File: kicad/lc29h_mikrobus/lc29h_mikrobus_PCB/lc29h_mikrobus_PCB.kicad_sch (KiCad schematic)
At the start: 43 parts, among them IC1 MIKROE-924, IC101 DS28E36BQ+U, IC102 74LVC1G3157GV,125, IC103 TXS0102DQER, J1 Conn_Coaxial, Q1 DMP3013SFV, Q101 BC856B-13-F, Q102 BSS123L, Q2 NPN, SW101 SW_Nidec_CAS-120A1, U101 LC29H

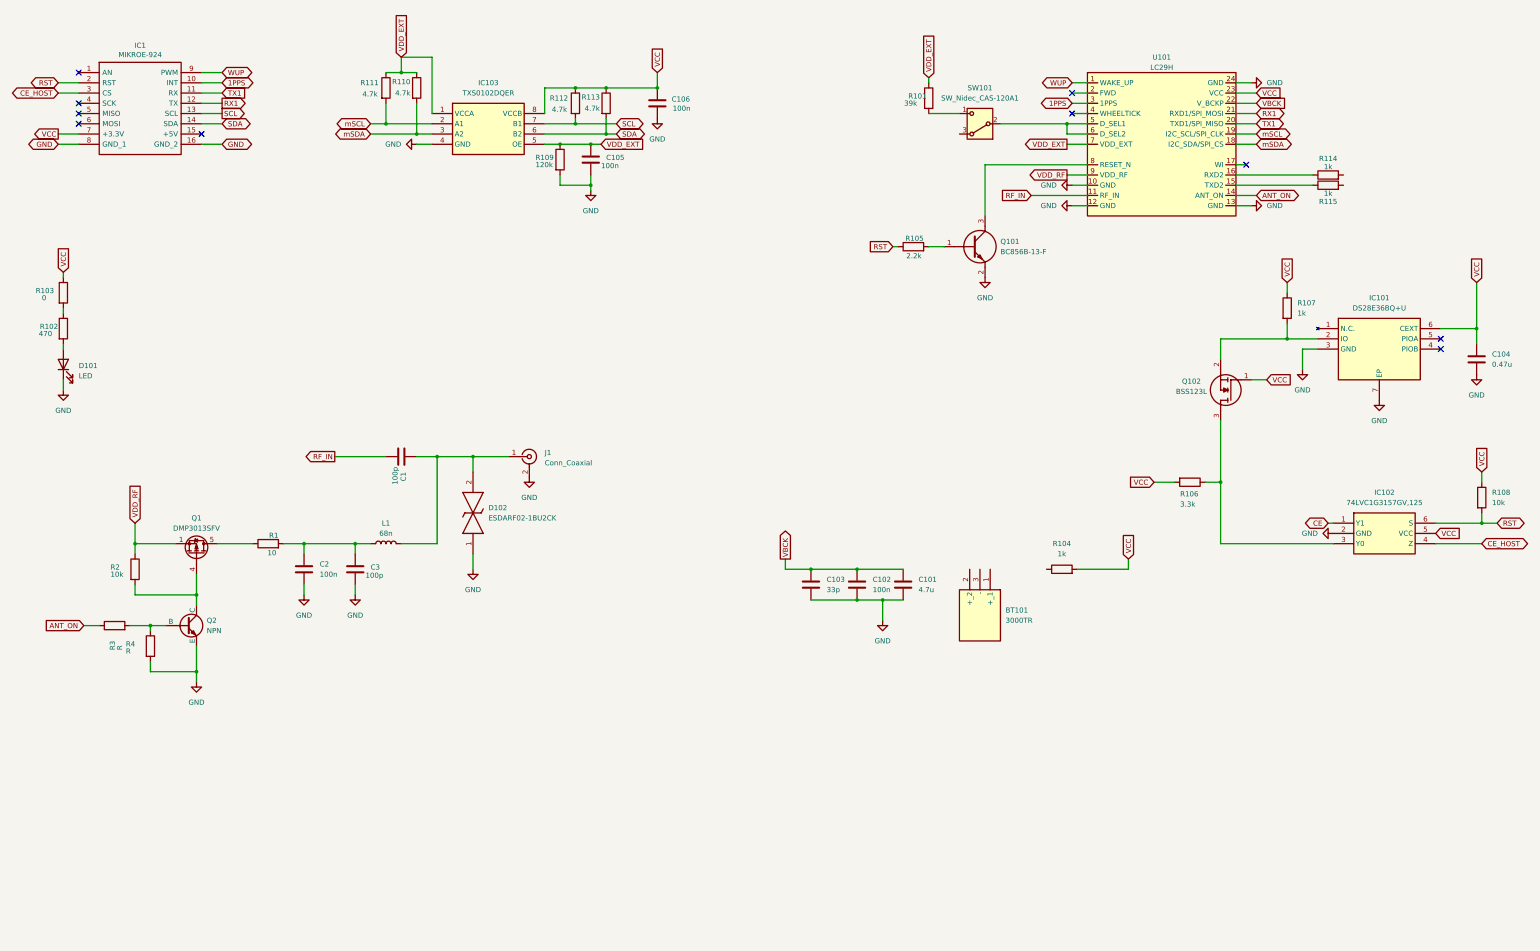
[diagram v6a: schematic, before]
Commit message: connecteur 3broches+ batterie
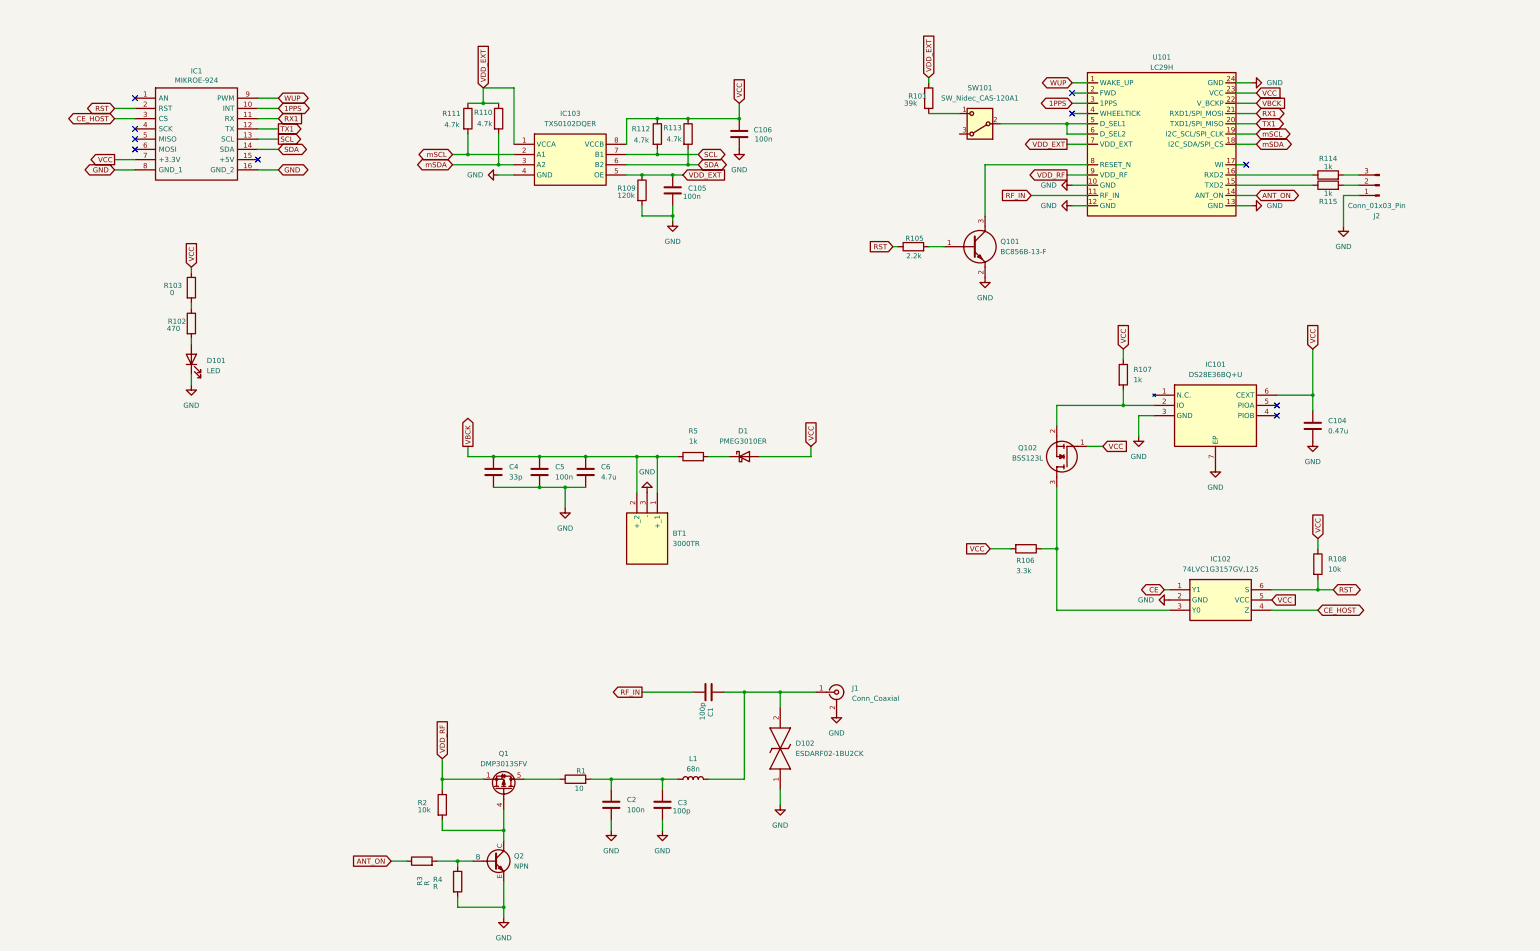
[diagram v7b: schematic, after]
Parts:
- removed BT101: 3000TR, 3000TR, symbol 3000TR:3000TR
- removed C101: 4.7u, symbol Device:C
- removed C102: 100n, symbol Device:C
- removed C103: 33p, symbol Device:C
- removed R104: 1k, symbol Device:R
- added BT1: 3000TR, 3000TR, symbol 3000TR:3000TR
- added C4: 33p, symbol Device:C
- added C5: 100n, symbol Device:C
- added C6: 4.7u, symbol Device:C
- added D1: PMEG3010ER, Diode_SMD:Nexperia_CFP3_SOD-123W, symbol Diode:PMEG3010ER
- added J2: Conn_01x03_Pin, symbol Connector:Conn_01x03_Pin
- added R5: 1k, symbol Device:R
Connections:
- net GND: now also BT1.3 (-), C4.2, C5.2, C6.2, J2.1 (Pin_1)
- net RX1: now also IC1.11 (RX); no longer IC1.12 (TX)
- net TX1: now also IC1.12 (TX); no longer IC1.11 (RX)
- net VBCK: now also BT1.1 (+_1), BT1.2 (+_2), C4.1, C5.1, C6.1, R5.1
- net VCC: now also D1.2 (A)
- net at R115.2: now also J2.2 (Pin_2)
- net at R114.2: now also J2.3 (Pin_3)
- new net: D1.1 (K), R5.2
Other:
- moved on the sheet: C1, C104, C105, C106, C2, C3, D101, D102, IC1, IC101, IC102, IC103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

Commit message: debut connexion pcb
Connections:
- net RX1: now also IC1.12 (TX); no longer IC1.11 (RX)
- net TX1: now also IC1.11 (RX); no longer IC1.12 (TX)
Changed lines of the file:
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@@
-		)
-	)
-	(global_label "TX1"
-		(shape output)
-		(at 93.98 50.8 0)
-		(effects
-			(font
-				(size 1.27 1.27)
-			)
-			(justify left)
-		)
-		(property "Intersheetrefs" "${INTERSHEET_REFS}"
-			(at 93.98 50.8 0)
-			(effects
-				(font
-					(size 1.27 1.27)
-				)
-				(hide yes)
-			)
 		)
 	)
@@
 	)
 	(global_label "RX1"
-		(shape bidirectional)
+		(shape input)
 		(at 336.55 46.99 0)
 		(fields_autoplaced yes)
@@
 		)
 		(property "Intersheetrefs" "${INTERSHEET_REFS}"
-			(at 343.5225 46.99 0)
+			(at 342.57 46.99 0)
 			(effects
 				(font
@@
 		)
 	)
+	(global_label "RX1"
+		(shape output)
+		(at 93.98 50.8 0)
+		(effects
+			(font
+				(size 1.27 1.27)
+			)
+			(justify left)
+		)
+		(property "Intersheetrefs" "${INTERSHEET_REFS}"
+			(at 93.98 50.8 0)
+			(effects
+				(font
+					(size 1.27 1.27)
+				)
+				(hide yes)
+			)
+		)
+	)
 	(global_label "TX1"
-		(shape bidirectional)
+		(shape output)
 		(at 336.55 49.53 0)
 		(fields_autoplaced yes)
@@
 		)
 		(property "Intersheetrefs" "${INTERSHEET_REFS}"
-			(at 343.2201 49.53 0)
+			(at 342.2676 49.53 0)
 			(effects
 				(font
@@
 		)
 	)
-	(global_label "RX1"
+	(global_label "VCC"
+		(shape input)
+		(at 72.39 85.09 90)
+		(fields_autoplaced yes)
+		(effects
+			(font
+				(size 1.27 1.27)
+			)
+			(justify left)
+		)
+		(property "Intersheetrefs" "${INTERSHEET_REFS}"
+			(at 72.39 79.1304 90)
+			(effects
+				(font
+					(size 1.27 1.27)
+				)
+				(justify left)
+				(hide yes)
+			)
+		)
+	)
+	(global_label "TX1"
 		(shape input)
 		(at 93.98 48.26 0)
@@
 				(hide yes)
 			)
-		)
-	)
-	(global_label "VCC"
-		(shape input)
-		(at 72.39 85.09 90)
-		(fields_autoplaced yes)
-		(effects
-			(font
-				(size 1.27 1.27)
-			)
-			(justify left)
-		)
-		(property "Intersheetrefs" "${INTERSHEET_REFS}"
-			(at 72.39 79.1304 90)
-			(effects
-				(font
-					(size 1.27 1.27)
-				)
-				(justify left)
-				(hide yes)
-			)
